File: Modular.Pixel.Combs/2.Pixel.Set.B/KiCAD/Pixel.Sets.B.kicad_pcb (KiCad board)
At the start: 2 copper layers, 78 x 78 mm, 20 parts

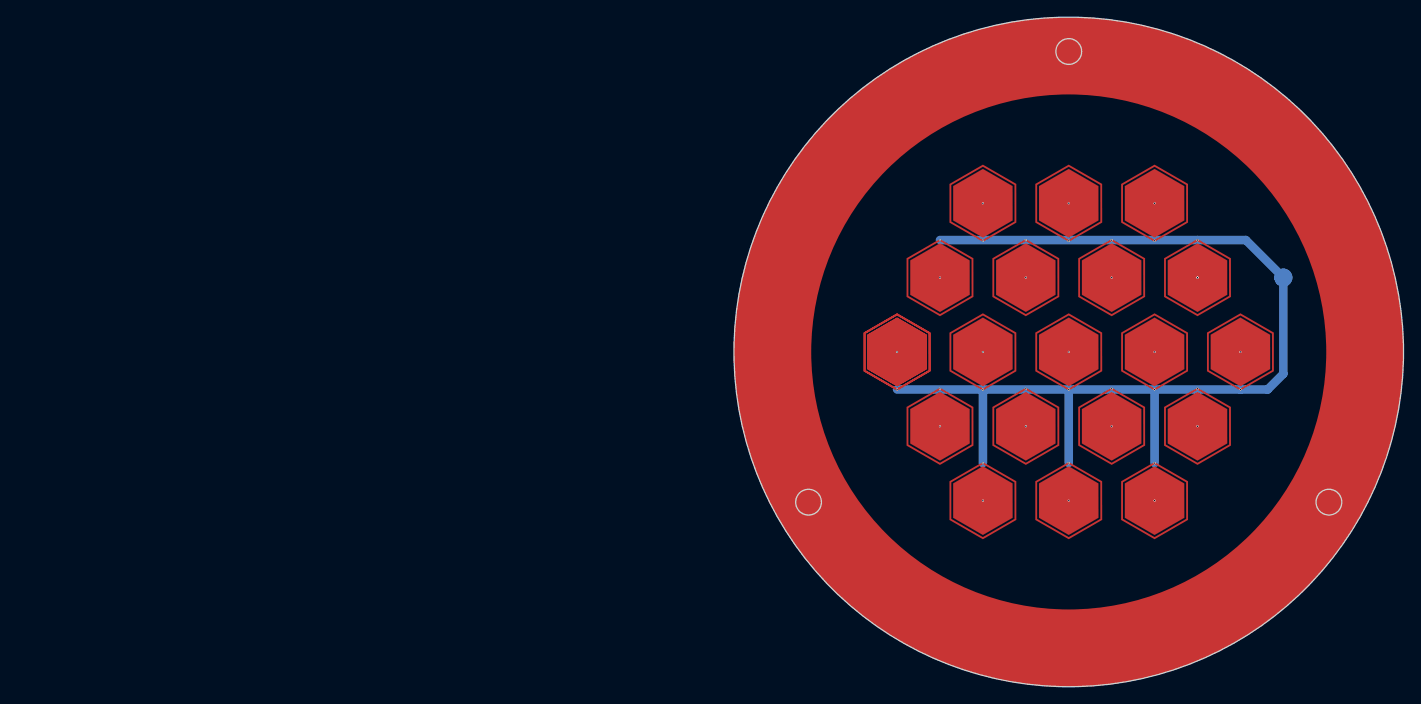
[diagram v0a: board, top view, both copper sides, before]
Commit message: Smoothed out Hexagon Pixels so that it Better Fits the Stencils
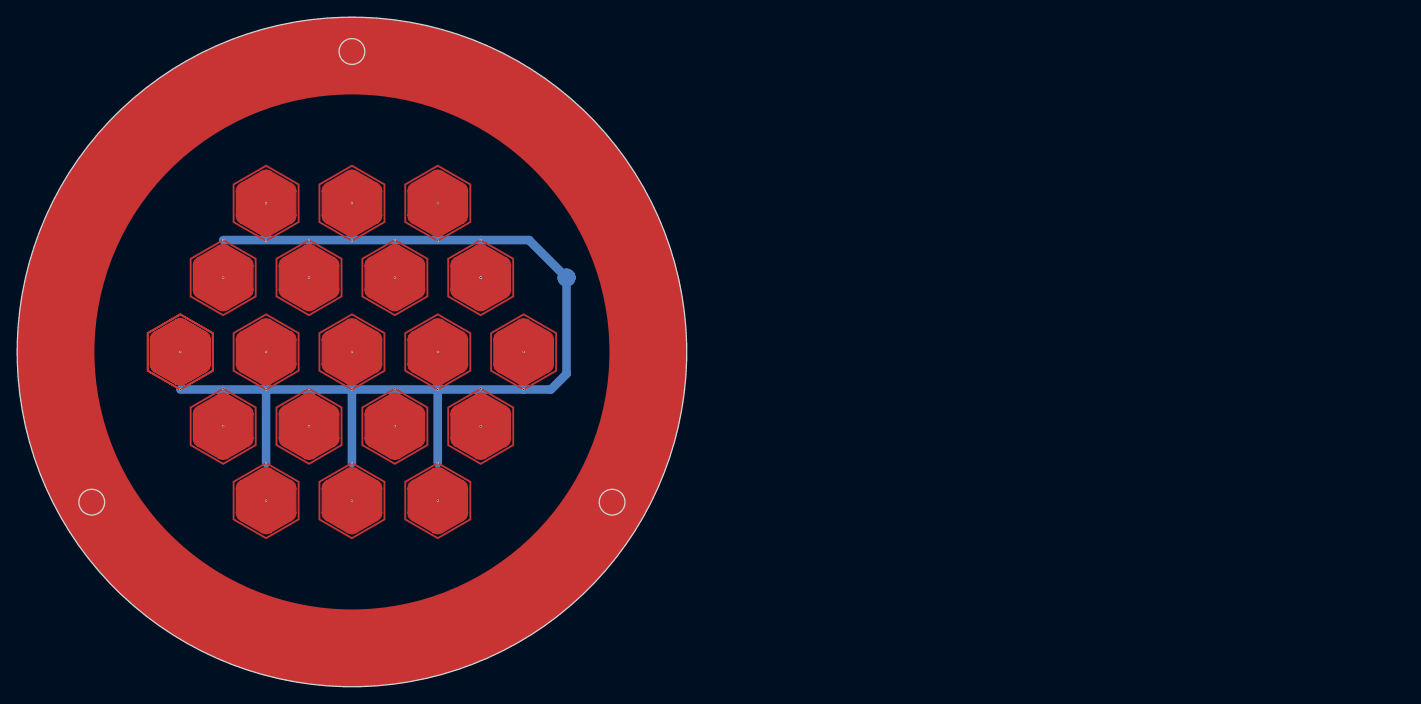
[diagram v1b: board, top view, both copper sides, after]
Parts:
- moved REF** 83.5 mm to (148.5, 58.3)
- moved REF**12 83.5 mm to (168.5, 58.3)
- moved REF**18 83.5 mm to (153.5, 67.0)
- moved REF**22 83.5 mm to (163.5, 67.0)
- moved REF**29 83.5 mm to (158.5, 75.6)
- moved REF**59 83.5 mm to (143.5, 49.6)
- moved REF**60 83.5 mm to (153.5, 49.6)
- moved REF**61 83.5 mm to (163.5, 49.6)
- moved REF**63 83.5 mm to (138.5, 41.0)
- moved REF**65 83.5 mm to (148.5, 41.0)
- moved REF**66 83.5 mm to (158.5, 41.0)
- moved REF**7 83.5 mm to (158.5, 58.3)
- moved REF**75 83.5 mm to (138.5, 58.3)
- moved REF**76 83.5 mm to (128.5, 58.3)
- moved REF**79 83.5 mm to (143.5, 67.0)
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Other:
- board text added: "Pixel Board B ::: May 2023 Alfredo Barajas Enriquez"
- board text removed: "Pixel Set B ::: May 2023 Alfredo Barajas Enriquez"

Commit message: Minor Fixes
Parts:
- added G***: LOGO, LOGO, B.Cu at (158.2, 88.2)
